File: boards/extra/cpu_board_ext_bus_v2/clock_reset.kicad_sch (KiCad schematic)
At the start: 8 parts, among them J2 EXT_CLK, J3 CPU_CLK_SEL, J4 BUS_CLK_SEL, X1 INT_CLK

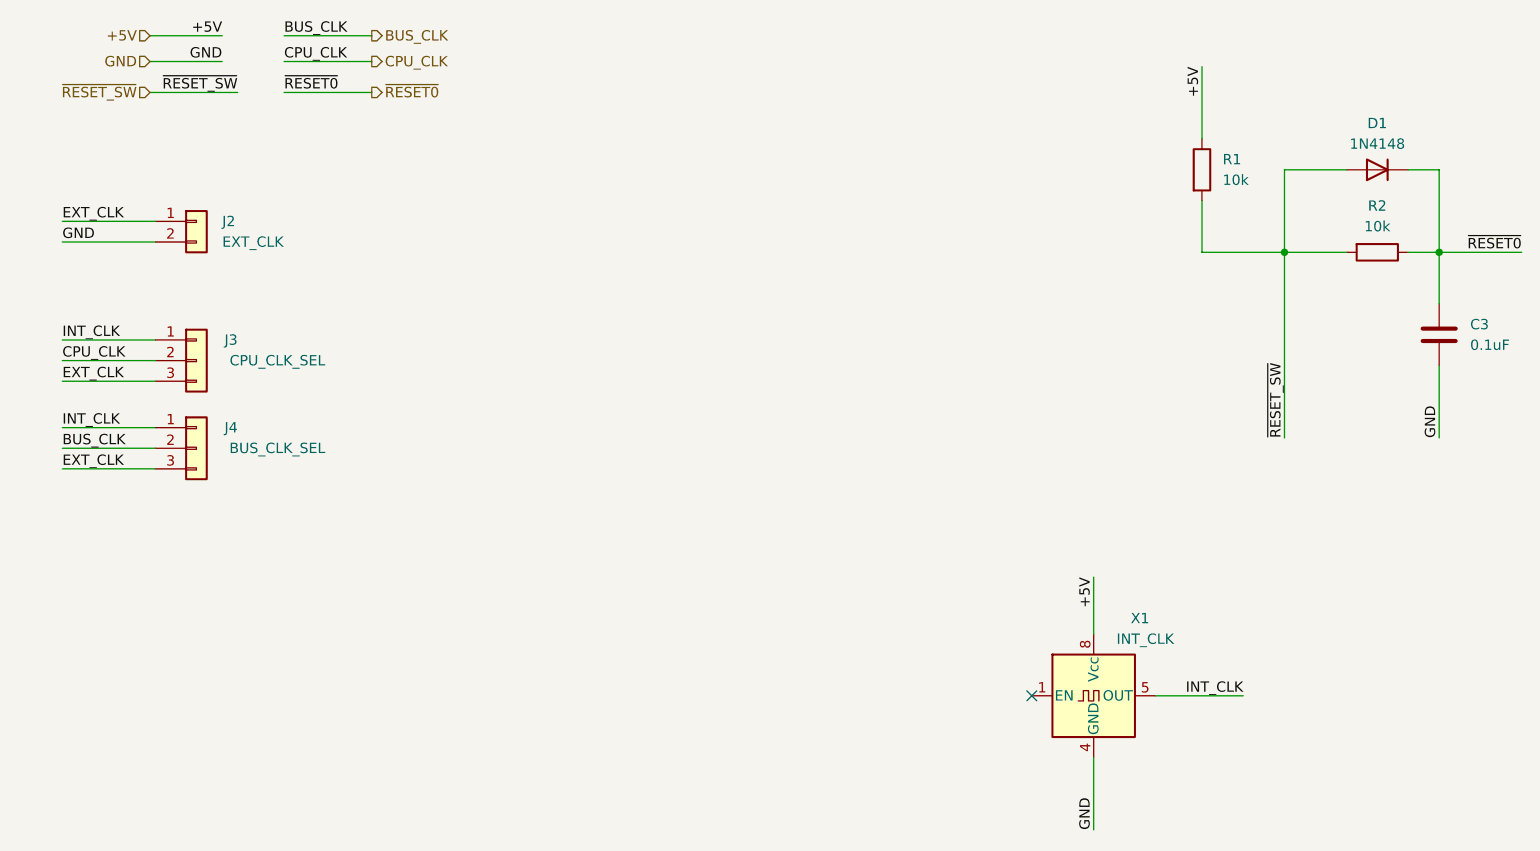
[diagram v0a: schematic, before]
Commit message: Updated CPU board V2 with extension bus
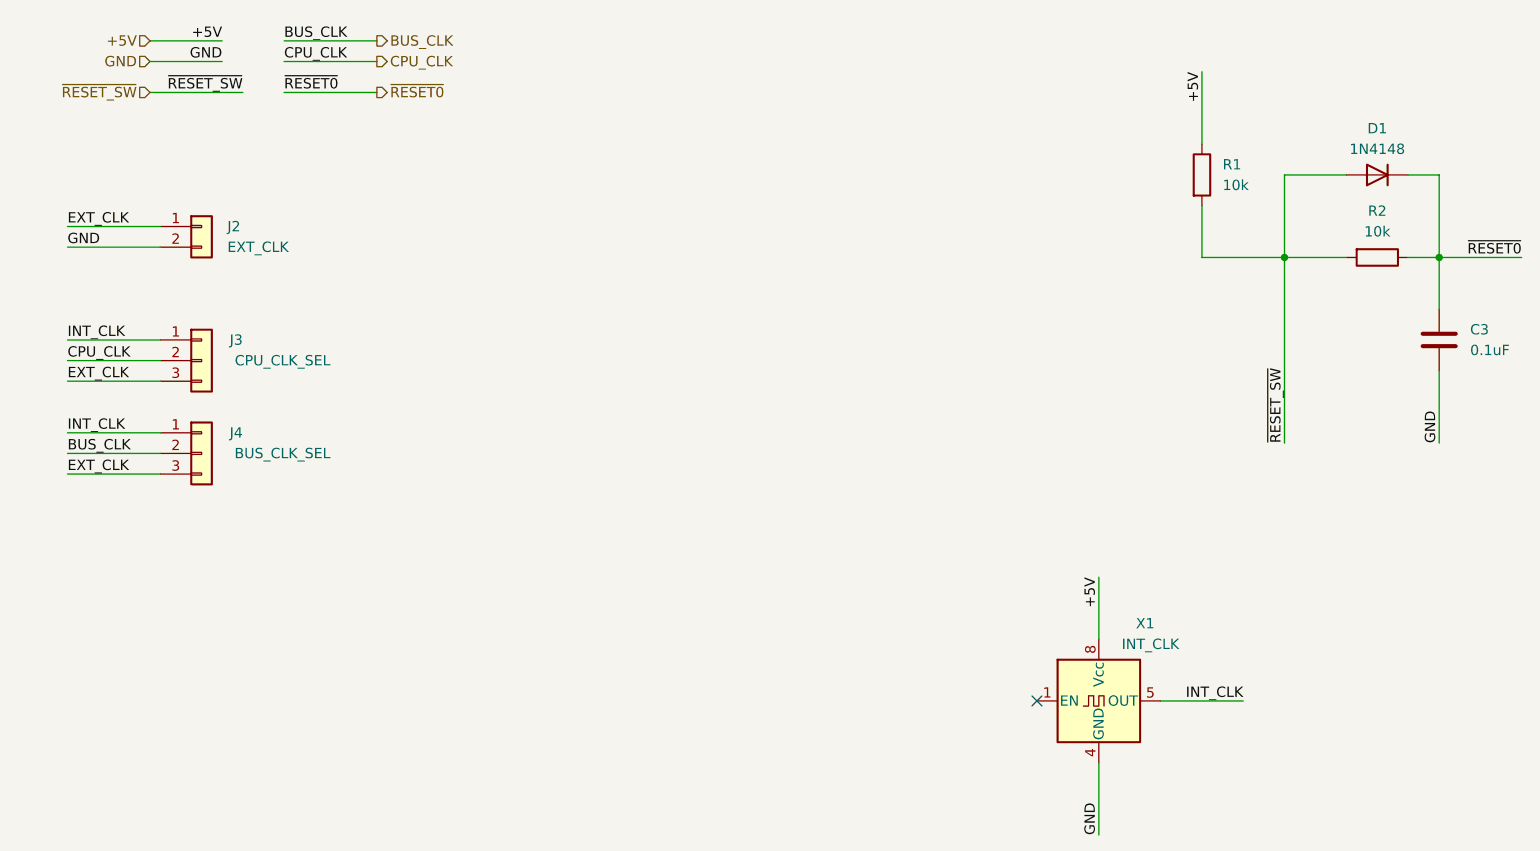
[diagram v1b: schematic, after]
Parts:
- R1, R2: MPN MFR3WSFTE73-10K -> MBA02040C1002FRP00; Manufacturer YAGEO -> Vishay Intertech
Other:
- moved on the sheet: C3, D1, J2, J3, J4, R1, R2, X1

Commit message: Extended CPU board update
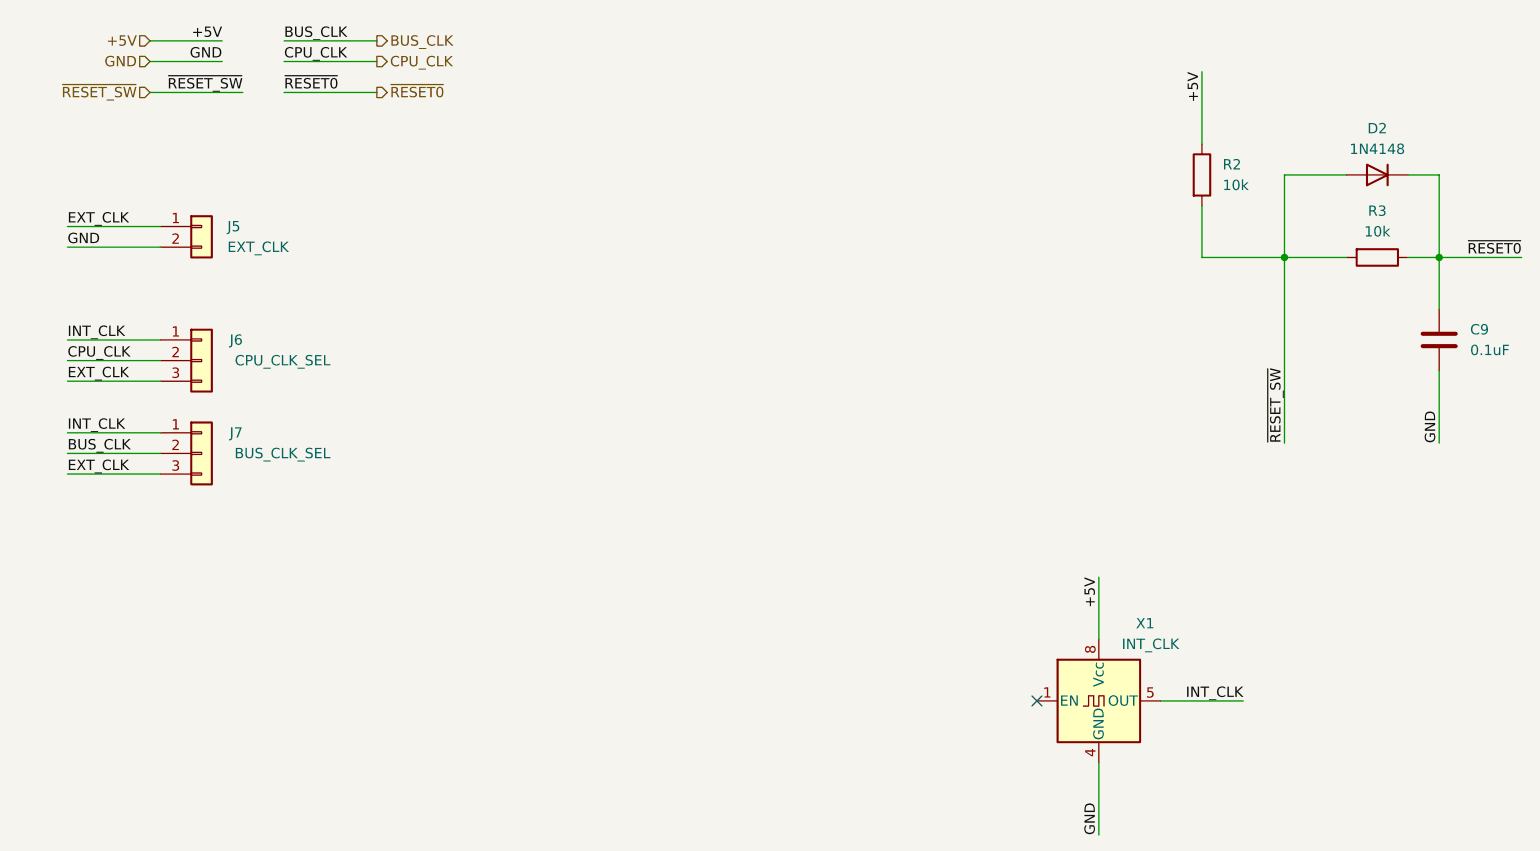
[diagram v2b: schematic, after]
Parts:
- X1: footprint Package_DIP:DIP-8_W7.62mm_Socket -> Oscillator:Oscillator_DIP-8
- renumbered C3 to C9, D1 to D2, J2 to J5, J3 to J6, J4 to J7, R1 to R2, R2 to R3
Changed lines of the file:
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@@
 (kicad_sch
-	(version 20231120)
+	(version 20250114)
 	(generator "eeschema")
-	(generator_version "8.0")
+	(generator_version "9.0")
 	(paper "A4")
 	(title_block
@@
 	(label "+5V"
 		(at 142.24 83.82 270)
-		(fields_autoplaced yes)
 		(effects
 			(font
@@
 	(label "CPU_CLK"
 		(at 41.91 20.32 0)
-		(fields_autoplaced yes)
 		(effects
 			(font
@@
 	(label "INT_CLK"
 		(at 15.24 54.61 0)
-		(fields_autoplaced yes)
 		(effects
 			(font
@@
 	(label "GND"
 		(at 34.29 20.32 180)
-		(fields_autoplaced yes)
 		(effects
 			(font
@@
 	(label "EXT_CLK"
 		(at 15.24 40.64 0)
-		(fields_autoplaced yes)
 		(effects
 			(font
@@
 	(label "GND"
 		(at 142.24 115.57 90)
-		(fields_autoplaced yes)
 		(effects
 			(font
@@
 	(label "INT_CLK"
 		(at 160.02 99.06 180)
-		(fields_autoplaced yes)
 		(effects
 			(font
@@
 	(label "+5V"
 		(at 34.29 17.78 180)
-		(fields_autoplaced yes)
 		(effects
 			(font
@@
 	(label "INT_CLK"
 		(at 15.24 66.04 0)
-		(fields_autoplaced yes)
 		(effects
 			(font
@@
 	(label "CPU_CLK"
 		(at 15.24 57.15 0)
-		(fields_autoplaced yes)
 		(effects
 			(font
@@
 	(label "EXT_CLK"
 		(at 15.24 59.69 0)
-		(fields_autoplaced yes)
 		(effects
 			(font
@@
 	(label "GND"
 		(at 15.24 43.18 0)
-		(fields_autoplaced yes)
 		(effects
 			(font
@@
 	(label "~{RESET_SW}"
 		(at 165.1 67.31 90)
-		(fields_autoplaced yes)
 		(effects
 			(font
@@
 	(label "+5V"
 		(at 154.94 21.59 270)
-		(fields_autoplaced yes)
 		(effects
 			(font
@@
 	(label "BUS_CLK"
 		(at 15.24 68.58 0)
-		(fields_autoplaced yes)
 		(effects
 			(font
@@
 	(label "GND"
 		(at 184.15 67.31 90)
-		(fields_autoplaced yes)
 		(effects
 			(font
@@
 	(label "EXT_CLK"
 		(at 15.24 71.12 0)
-		(fields_autoplaced yes)
 		(effects
 			(font
@@
 	(label "~{RESET0}"
 		(at 41.91 24.13 0)
-		(fields_autoplaced yes)
 		(effects
 			(font
@@
 	(label "~{RESET0}"
 		(at 194.31 44.45 180)
-		(fields_autoplaced yes)
 		(effects
 			(font
@@
 	(label "~{RESET_SW}"
 		(at 36.83 24.13 180)
-		(fields_autoplaced yes)
 		(effects
 			(font
@@
 	(label "BUS_CLK"
 		(at 41.91 17.78 0)
-		(fields_autoplaced yes)
 		(effects
 			(font
@@
 		(shape output)
 		(at 53.34 24.13 0)
-		(fields_autoplaced yes)
 		(effects
 			(font
@@
 		(shape output)
 		(at 53.34 17.78 0)
-		(fields_autoplaced yes)
 		(effects
 			(font
@@
 		(shape input)
 		(at 25.4 24.13 180)
-		(fields_autoplaced yes)
 		(effects
 			(font
@@
 		(shape input)
 		(at 25.4 20.32 180)
-		(fields_autoplaced yes)
 		(effects
 			(font
@@
 		(shape output)
 		(at 53.34 20.32 0)
-		(fields_autoplaced yes)
 		(effects
 			(font
@@
 		(shape input)
 		(at 25.4 17.78 180)
-		(fields_autoplaced yes)
 		(effects
 			(font
@@
 			)
 		)
-		(property "Footprint" "Package_DIP:DIP-8_W7.62mm_Socket"
+		(property "Footprint" "Oscillator:Oscillator_DIP-8"
 			(at 153.67 107.95 0)
 			(effects
@@
 			)
 		)
-		(property "Description" "Phosphor bronze 7.62mm DIP-8 IC / Transistor Socket ROHS "
+		(property "Description" "Crystal Clock Oscillator, DIP8-style metal package"
 			(at 142.24 99.06 0)
 			(effects
@@
 		(dnp no)
 		(fields_autoplaced yes)
-		(property "Reference" "R2"
+		(property "Reference" "R3"
 			(at 176.53 38.735 90)
 			(effects
@@
 		(dnp no)
 		(fields_autoplaced yes)
-		(property "Reference" "C3"
+		(property "Reference" "C9"
 			(at 187.96 53.34 0)
 			(effects
@@
 		(on_board yes)
 		(dnp no)
-		(property "Reference" "J3"
+		(property "Reference" "J6"
 			(at 36.83 54.61 0)
 			(effects
@@
 		(dnp no)
 		(fields_autoplaced yes)
-		(property "Reference" "D1"
+		(property "Reference" "D2"
 			(at 176.53 28.575 0)
 			(effects
@@
 		(dnp no)
 		(fields_autoplaced yes)
-		(property "Reference" "R1"
+		(property "Reference" "R2"
 			(at 157.48 33.02 0)
 			(effects
@@
 		(on_board yes)
 		(dnp no)
-		(property "Reference" "J4"
+		(property "Reference" "J7"
 			(at 36.83 66.04 0)
 			(effects
@@
 		(dnp no)
 		(fields_autoplaced yes)
-		(property "Reference" "J2"
+		(property "Reference" "J5"
 			(at 34.925 40.64 0)
 			(effects
